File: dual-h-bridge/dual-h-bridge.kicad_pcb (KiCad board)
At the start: 2 copper layers, 40.9 x 101.5 mm, 79 parts, among them J1 Motor0, J2 Motor1, J3 BATT, J4 MCU, M0.Fow_Gate Motor0.FOW_GATE, M0.Rev_Gate Motor0.REV_GATE, M1.Fow_Gate Motor1.FOW_GATE, M1.Rev_Gate Motor1.REV_GATE, Q1 2N3904, Q10 VN2222L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

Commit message: minor changes to back silkscreen
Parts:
- added REF**: KiCad-Logo2_5mm_SilkScreen, Symbol:KiCad-Logo2_5mm_SilkScreen, B.Cu at (212.6, 80.0)
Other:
- board text added: "Designed by George Sleen"
- board text added: "https://github.com/ enph253-2025-team5/ dual-h-bridge-pcb"
- board text removed: "GS"

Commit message: Update to right angle motor connectors
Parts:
- J1, J2: footprint Connector_JST:JST_XH_B2B-XH-A_1x02_P2.50mm_Vertical -> GS_Connectors:JST_XH_S2B-XH-A-1_1x02_P2.50mm_Horizontal
- moved J2 1.97 mm to (225.4, 67.1)
- moved J1 1.76 mm to (200.2, 64.7)

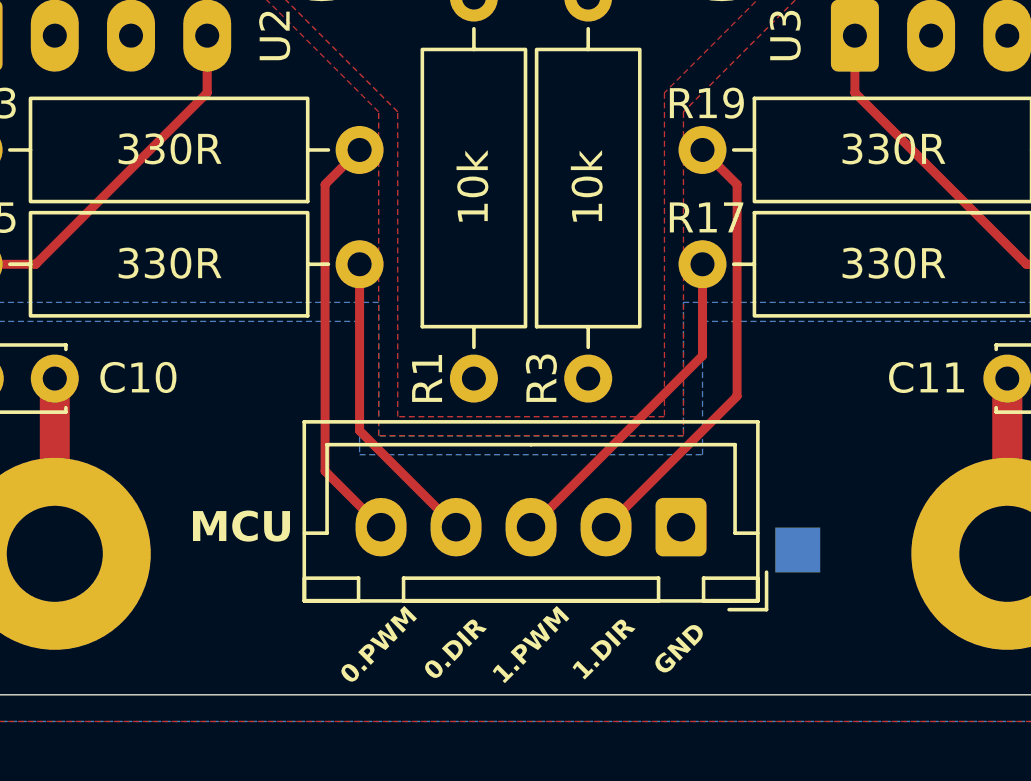
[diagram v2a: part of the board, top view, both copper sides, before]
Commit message: Change to new connector standard
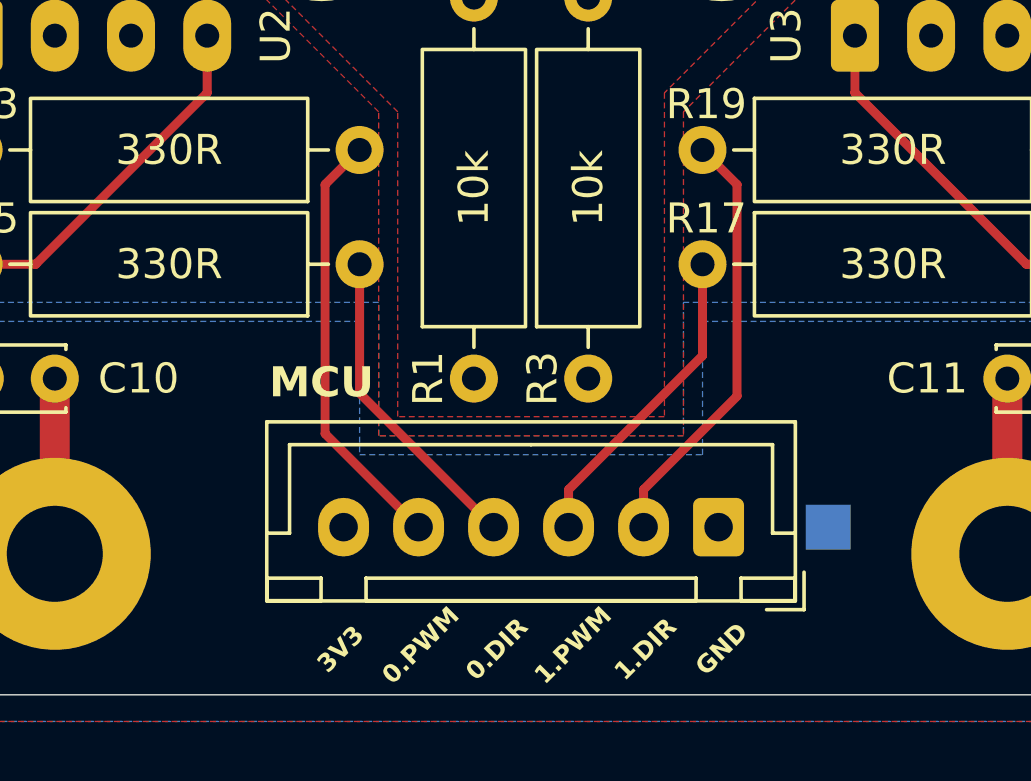
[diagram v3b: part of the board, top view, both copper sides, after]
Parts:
- J4: footprint Connector_JST:JST_XH_B5B-XH-A_1x05_P2.50mm_Vertical -> Connector_JST:JST_XH_B6B-XH-A_1x06_P2.50mm_Vertical
- moved MCU.GND 1.27 mm to (222.6, 136.3)
- moved J4 1.25 mm to (219.0, 136.3)
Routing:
- net /MCU.PWM0: track 13.8 -> 14.3 mm
- net /MCU.PWM1: track 11.1 -> 10.6 mm
- net /MCU.DIR1: track 14.9 -> 14.3 mm
- net /MCU.DIR0: track 10.1 -> 10.6 mm
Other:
- board text added: "3V3"
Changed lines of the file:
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@@
 		)
 	)
-	(footprint "Connector_JST:JST_XH_B5B-XH-A_1x05_P2.50mm_Vertical"
+	(footprint "Connector_JST:JST_XH_B6B-XH-A_1x06_P2.50mm_Vertical"
 		(layer "F.Cu")
-		(at 217.725 136.271 180)
-		(descr "JST XH series connector, B5B-XH-A (http://www.jst-mfg.com/product/pdf/eng/eXH.pdf), generated with kicad-footprint-generator")
+		(at 218.975 136.271 180)
+		(descr "JST XH series connector, B6B-XH-A (http://www.jst-mfg.com/product/pdf/eng/eXH.pdf), generated with kicad-footprint-generator")
 		(tags "connector JST XH vertical")
 		(property "Reference" "J4"
-			(at 5 -3.55 0)
-			(layer "F.Fab")
+			(at 6.25 -3.55 180)
+			(layer "F.SilkS")
 			(hide yes)
 			(effects
@@
 		)
 		(property "Value" "MCU"
-			(at 14.652 0 0)
+			(at 13.235 4.826 180)
 			(layer "F.SilkS")
 			(effects
@@
 		)
 		(property "Datasheet" ""
-			(at 0 0 0)
+			(at 0 0 180)
 			(layer "F.Fab")
 			(hide yes)
@@
 			)
 		)
-		(property "Description" "Generic connector, single row, 01x05, script generated"
-			(at 0 0 0)
+		(property "Description" ""
+			(at 0 0 180)
 			(layer "F.Fab")
 			(hide yes)
@@
 		(attr through_hole)
 		(fp_line
-			(start 12.56 3.51)
-			(end 12.56 -2.46)
+			(start 15.06 3.51)
+			(end 15.06 -2.46)
 			(stroke
 				(width 0.12)
@@
 		)
 		(fp_line
-			(start 12.56 -2.46)
+			(start 15.06 -2.46)
 			(end -2.56 -2.46)
 			(stroke
@@
 		)
 		(fp_line
-			(start 12.55 -0.2)
-			(end 11.8 -0.2)
+			(start 15.05 -0.2)
+			(end 14.3 -0.2)
 			(stroke
 				(width 0.12)
@@
 		)
 		(fp_line
-			(start 12.55 -1.7)
-			(end 12.55 -2.45)
+			(start 15.05 -1.7)
+			(end 15.05 -2.45)
 			(stroke
 				(width 0.12)
@@
 		)
 		(fp_line
-			(start 12.55 -2.45)
-			(end 10.75 -2.45)
+			(start 15.05 -2.45)
+			(end 13.25 -2.45)
 			(stroke
 				(width 0.12)
@@
 		)
 		(fp_line
-			(start 11.8 2.75)
-			(end 5 2.75)
+			(start 14.3 2.75)
+			(end 6.25 2.75)
 			(stroke
 				(width 0.12)
@@
 		)
 		(fp_line
-			(start 11.8 -0.2)
-			(end 11.8 2.75)
+			(start 14.3 -0.2)
+			(end 14.3 2.75)
 			(stroke
 				(width 0.12)
@@
 		)
 		(fp_line
-			(start 10.75 -1.7)
-			(end 12.55 -1.7)
+			(start 13.25 -1.7)
+			(end 15.05 -1.7)
 			(stroke
 				(width 0.12)
@@
 		)
 		(fp_line
-			(start 10.75 -2.45)
-			(end 10.75 -1.7)
+			(start 13.25 -2.45)
+			(end 13.25 -1.7)
 			(stroke
 				(width 0.12)
@@
 		)
 		(fp_line
-			(start 9.25 -1.7)
-			(end 9.25 -2.45)
+			(start 11.75 -1.7)
+			(end 11.75 -2.45)
 			(stroke
 				(width 0.12)
@@
 		)
 		(fp_line
-			(start 9.25 -2.45)
+			(start 11.75 -2.45)
 			(end 0.75 -2.45)
 			(stroke
@@
 		(fp_line
 			(start 0.75 -1.7)
-			(end 9.25 -1.7)
+			(end 11.75 -1.7)
 			(stroke
 				(width 0.12)
@@
 		(fp_line
 			(start -1.8 2.75)
-			(end 5 2.75)
+			(end 6.25 2.75)
 			(stroke
 				(width 0.12)
@@
 		(fp_line
 			(start -2.56 3.51)
-			(end 12.56 3.51)
+			(end 15.06 3.51)
 			(stroke
 				(width 0.12)
@@
 		)
 		(fp_line
-			(start 12.95 3.9)
-			(end 12.95 -2.85)
+			(start 15.45 3.9)
+			(end 15.45 -2.85)
 			(stroke
 				(width 0.05)
@@
 		)
 		(fp_line
-			(start 12.95 -2.85)
+			(start 15.45 -2.85)
 			(end -2.95 -2.85)
 			(stroke
@@
 		(fp_line
 			(start -2.95 3.9)
-			(end 12.95 3.9)
+			(end 15.45 3.9)
 			(stroke
 				(width 0.05)
@@
 		)
 		(fp_line
-			(start 12.45 3.4)
-			(end 12.45 -2.35)
+			(start 14.95 3.4)
+			(end 14.95 -2.35)
 			(stroke
 				(width 0.1)
@@
 		)
 		(fp_line
-			(start 12.45 -2.35)
+			(start 14.95 -2.35)
 			(end -2.45 -2.35)
 			(stroke
@@
 		(fp_line
 			(start -2.45 3.4)
-			(end 12.45 3.4)
+			(end 14.95 3.4)
 			(stroke
 				(width 0.1)
@@
 		)
 		(fp_text user "${REFERENCE}"
-			(at 5 2.7 0)
+			(at 6.25 2.7 180)
 			(layer "F.Fab")
 			(effects
@@
 			(pintype "passive")
 		)
+		(pad "6" thru_hole oval
+			(at 12.5 0 180)
+			(size 1.7 1.95)
+			(drill 0.95)
+			(layers "*.Cu" "*.Mask")
+			(remove_unused_layers no)
+		)
 		(embedded_fonts no)
-		(model "${KICAD9_3DMODEL_DIR}/Connector_JST.3dshapes/JST_XH_B5B-XH-A_1x05_P2.50mm_Vertical.step"
+		(model "${KICAD9_3DMODEL_DIR}/Connector_JST.3dshapes/JST_XH_B6B-XH-A_1x06_P2.50mm_Vertical.step"
 			(offset
 				(xyz 0 0 0)
@@
 	(footprint "TestPoint:TestPoint_Pad_1.5x1.5mm"
 		(layer "B.Cu")
-		(at 221.615 137.033 180)
+		(at 222.631 136.271 180)
 		(descr "SMD rectangular pad as test Point, square 1.5mm side length")
 		(tags "test point SMD pad rectangle square")
@@
 	)
 	(gr_text "0.PWM"
-		(at 207.645 140.208 45)
+		(at 209.042 140.208 45)
 		(layer "F.SilkS")
 		(effects
@@
 	)
 	(gr_text "1.DIR"
-		(at 215.138 140.335 45)
+		(at 216.535 140.335 45)
+		(layer "F.SilkS")
+		(effects
+			(font
+				(size 0.6 0.6)
+				(thickness 0.15)
+				(bold yes)
+			)
+		)
+	)
+	(gr_text "3V3"
+		(at 206.375 140.335 45)
 		(layer "F.SilkS")
 		(effects
@@
 	)
 	(gr_text "GND"
-		(at 217.678 140.335 45)
+		(at 219.075 140.335 45)
 		(layer "F.SilkS")
 		(effects
@@
 	)
 	(gr_text "1.PWM"
-		(at 212.725 140.208 45)
+		(at 214.122 140.208 45)
 		(layer "F.SilkS")
 		(effects
@@
 	)
 	(gr_text "0.DIR"
-		(at 210.185 140.335 45)
+		(at 211.582 140.335 45)
 		(layer "F.SilkS")
 		(effects
@@
 	)
 	(gr_text "GND"
-		(at 217.805 137.922 90)
+		(at 218.948 137.922 90)
 		(layer "B.SilkS")
 		(effects
@@
 		)
 	)
+	(gr_text "3V3"
+		(at 206.502 137.795 90)
+		(layer "B.SilkS")
+		(effects
+			(font
+				(size 0.6 0.6)
+				(thickness 0.15)
+				(bold yes)
+			)
+			(justify left mirror)
+		)
+	)
 	(gr_text "PWM Magnitude: ~ 100 Hz\n"
 		(at 212.598 133.985 0)
@@
 	)
 	(gr_text "1.DIR"
-		(at 215.265 137.922 90)
+		(at 216.408 137.922 90)
 		(layer "B.SilkS")
 		(effects
@@
 	)
 	(gr_text "0.PWM"
-		(at 207.772 137.795 90)
+		(at 208.915 137.795 90)
 		(layer "B.SilkS")
 		(effects
@@
 	)
 	(gr_text "0.DIR"
-		(at 210.312 137.922 90)
+		(at 211.455 137.922 90)
 		(layer "B.SilkS")
 		(effects
@@
 	)
 	(gr_text "1.PWM"
-		(at 212.852 137.795 90)
+		(at 213.995 137.795 90)
 		(layer "B.SilkS")
 		(effects
@@
 	)
 	(segment
-		(start 205.859 134.405)
+		(start 207.01 123.698)
 		(end 205.859 124.849)
 		(width 0.3)
@@
 	)
 	(segment
-		(start 207.01 123.698)
-		(end 205.859 124.849)
+		(start 205.859 133.155)
+		(end 208.975 136.271)
 		(width 0.3)
 		(layer "F.Cu")
@@
 	)
 	(segment
-		(start 207.725 136.271)
-		(end 205.859 134.405)
+		(start 205.859 124.849)
+		(end 205.859 133.155)
 		(width 0.3)
 		(layer "F.Cu")
@@
 	)
 	(segment
-		(start 207.01 133.056)
-		(end 210.225 136.271)
+		(start 211.475 136.271)
+		(end 207.01 131.806)
 		(width 0.3)
 		(layer "F.Cu")
@@
 	)
 	(segment
-		(start 207.01 127.508)
-		(end 207.01 133.056)
+		(start 207.01 131.806)
+		(end 207.01 127.508)
 		(width 0.3)
 		(layer "F.Cu")
@@
 	)
 	(segment
-		(start 212.725 136.271)
-		(end 218.44 130.556)
+		(start 218.44 130.556)
+		(end 213.975 135.021)
+		(width 0.3)
+		(layer "F.Cu")
+		(net 37)
+	)
+	(segment
+		(start 213.975 135.021)
+		(end 213.975 136.271)
 		(width 0.3)
 		(layer "F.Cu")
@@
 	)
 	(segment
-		(start 215.225 136.271)
-		(end 219.591 131.905)
+		(start 219.591 124.849)
+		(end 218.44 123.698)
 		(width 0.3)
 		(layer "F.Cu")
@@
 	)
 	(segment
-		(start 219.591 124.849)
-		(end 218.44 123.698)
+		(start 219.591 131.905)
+		(end 216.475 135.021)
+		(width 0.3)
+		(layer "F.Cu")
+		(net 41)
+	)
+	(segment
+		(start 216.475 135.021)
+		(end 216.475 136.271)
 		(width 0.3)
 		(layer "F.Cu")
